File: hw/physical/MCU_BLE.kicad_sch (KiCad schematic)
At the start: 30 parts, among them SW201 RotaryEncoder_Switch, U1 nRF52840-QIAA, U5 MX25R3235FM1IL0, Y1 32M, Y2 32.768k

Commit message: - Consolidate POWER and BATTERY pages - Updated 1.8V SYS REG to low Iq option - Replaced LoRA module with SemTech transceiver - Adding latest nRF datasheet
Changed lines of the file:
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@@
 		(dnp no)
 		(property "Reference" "U1"
-			(at 199.39 57.15 0)
+			(at 202.946 60.452 0)
 			(effects
 				(font
@@
 		)
 		(property "Value" "nRF52840-QIAA"
-			(at 199.39 59.69 0)
+			(at 202.946 62.992 0)
 			(effects
 				(font

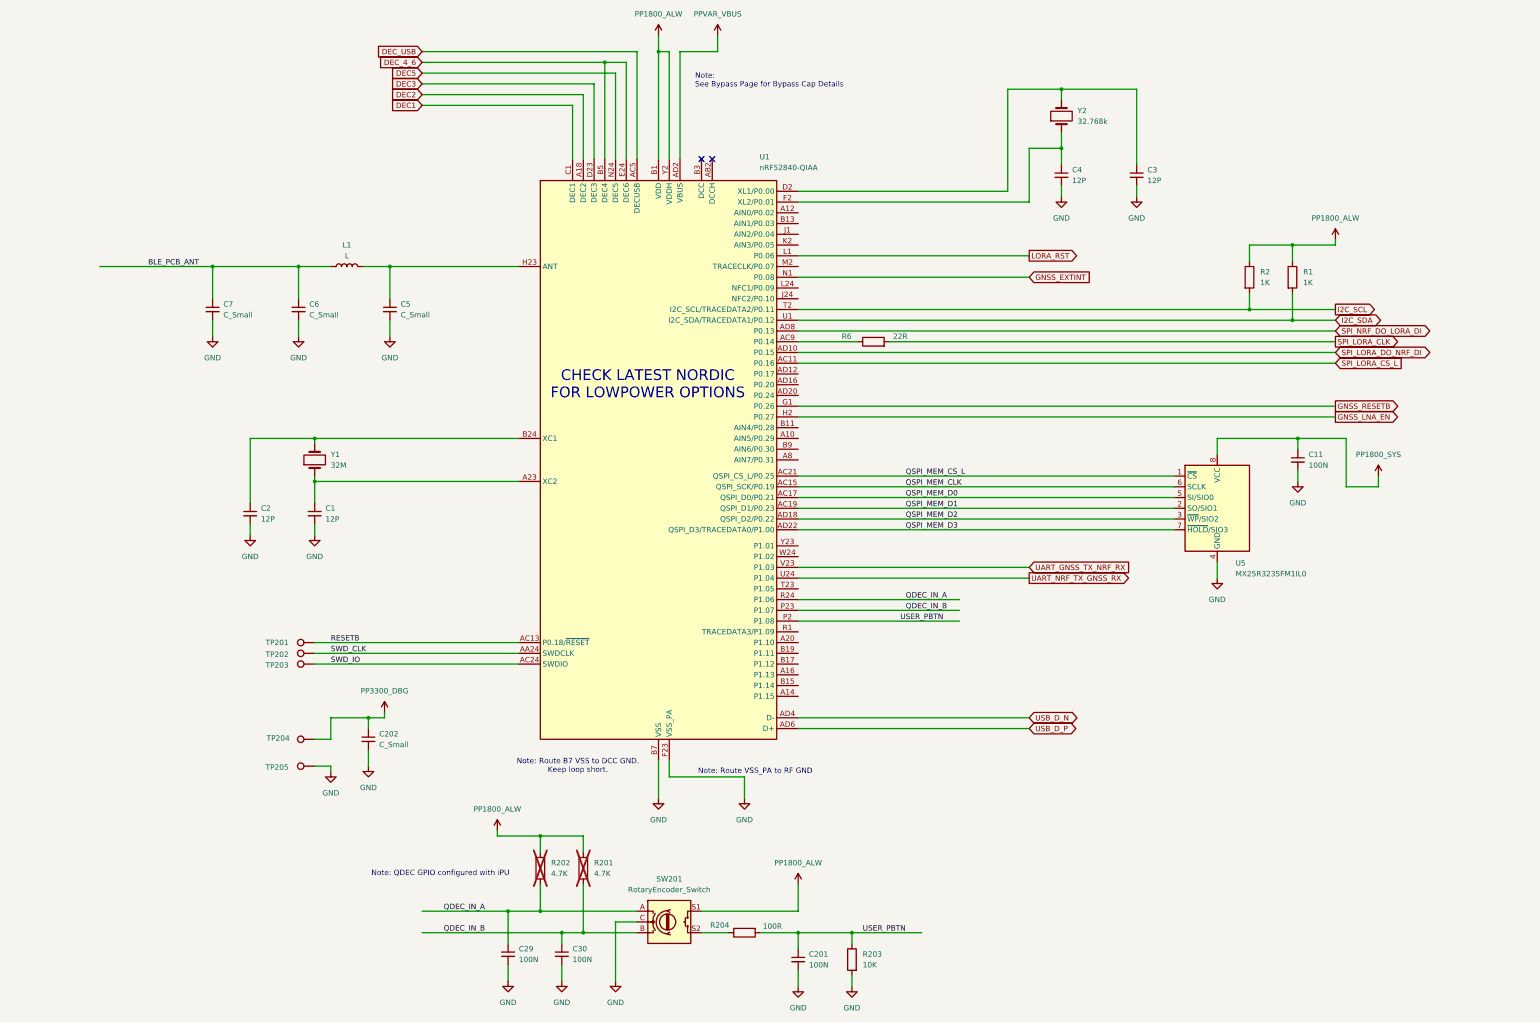
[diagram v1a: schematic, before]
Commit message: Adding nRF54L10 schematic library component. Redrew MCU page with nRF54L10 and rearranged or changed net labels and global labels.
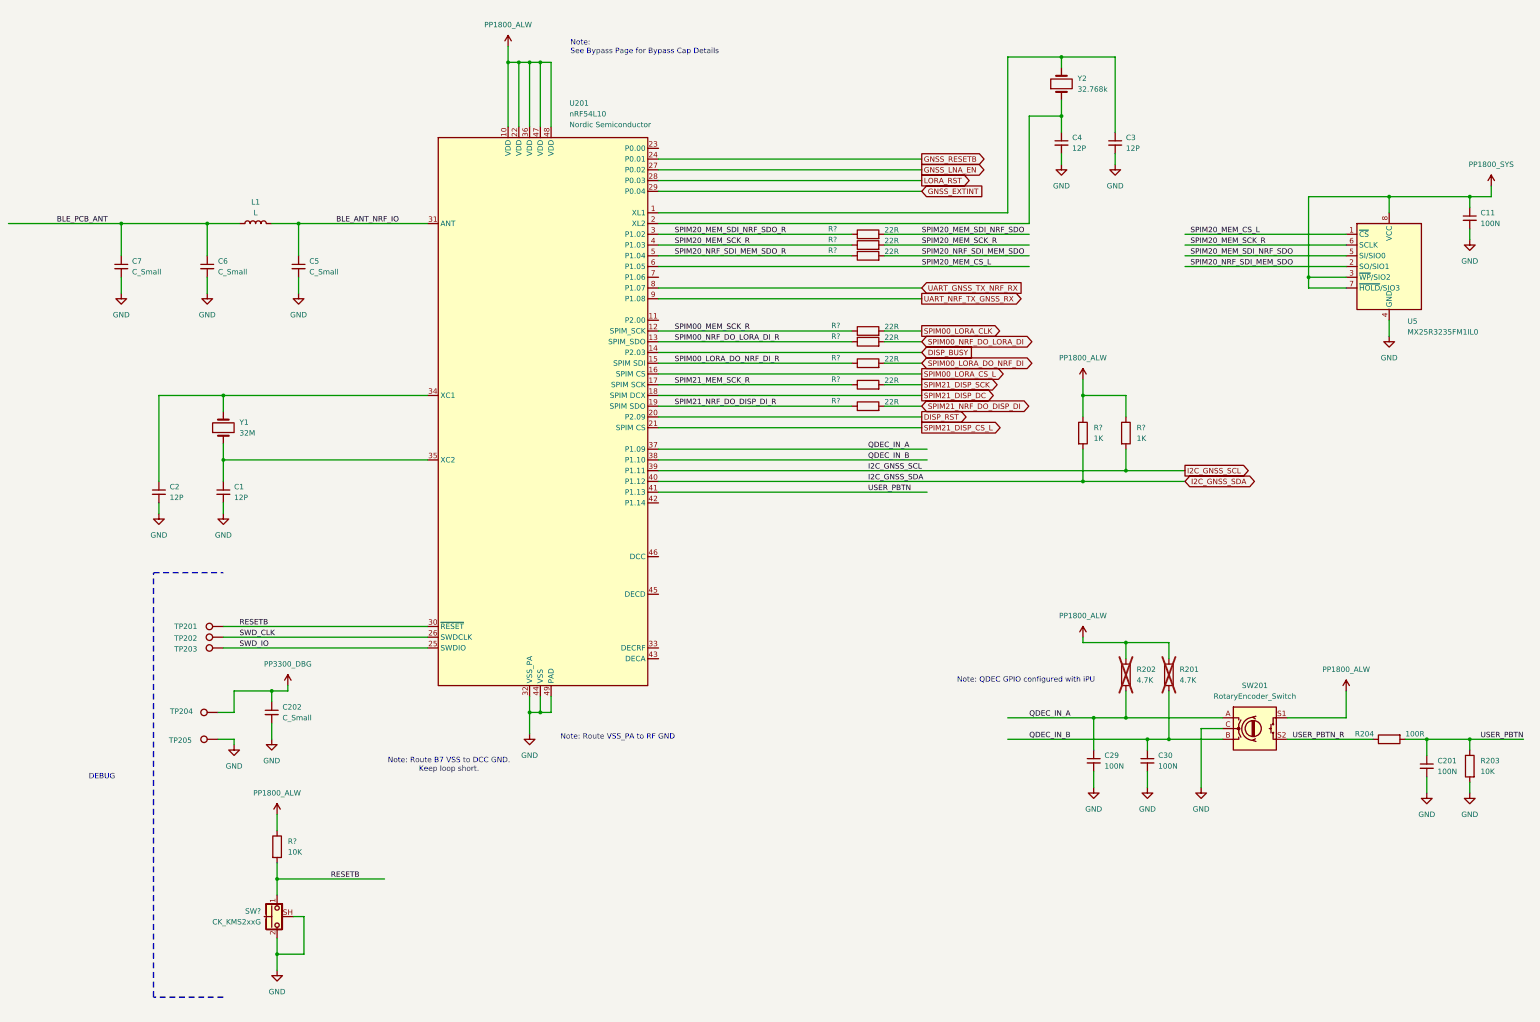
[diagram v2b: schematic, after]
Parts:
- removed R1, R2: 1K, symbol Device:R
- removed R6: 22R, symbol Device:R
- removed U1: nRF52840-QIAA, Package_DFN_QFN:Nordic_AQFN-73-1EP_7x7mm_P0.5mm, symbol MCU_Nordic:nRF52840
- added R? (x2): 1K, symbol Device:R
- added R? (x8): 22R, symbol Device:R
- added R?: 10K, symbol Device:R
- added SW?: CK_KMS2xxG, Button_Switch_SMD:SW_SPST_CK_KMS2xxGP, symbol Switch:CK_KMS2xxG
- added U201: nRF54L10, Package_DFN_QFN:QFN-48-1EP_6x6mm_P0.4mm_EP4.6x4.6mm, symbol nRF54L:nRF54L10
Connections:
- net QSPI_MEM_D2 is gone; now on net PP1800_SYS: U5.3 (~{WP}/SIO2)
- net QSPI_MEM_D3 is gone; now on net PP1800_SYS: U5.7 (~{HOLD}/SIO3)
- net GND: now also SW?.2, SW?.SH (B), U201.32 (VSS_PA), U201.44 (VSS), U201.49 (PAD)
- net GNSS_EXTINT: now also U201.29 (P0.04)
- net GNSS_LNA_EN: now also U201.27 (P0.02)
- net GNSS_RESETB: now also U201.24 (P0.01)
- net LORA_RST: now also U201.28 (P0.03)
- net PP1800_ALW: now also R?.1, R?.1, R?.1, U201.10 (VDD), U201.22 (VDD), U201.36 (VDD), U201.47 (VDD), U201.48 (VDD)
- net QDEC_IN_A: now also U201.37 (P1.09)
- net QDEC_IN_B: now also U201.38 (P1.10)
- net RESETB: now also R?.2, SW?.1, U201.30 (~{RESET})
- net SWD_CLK: now also U201.26 (SWDCLK)
- net SWD_IO: now also U201.25 (SWDIO)
- net UART_GNSS_TX_NRF_RX: now also U201.8 (P1.07)
- net UART_NRF_TX_GNSS_RX: now also U201.9 (P1.08)
- net USER_PBTN: now also U201.41 (P1.13)
- net at C1.1, Y1.1: now also U201.35 (XC2)
- net at C2.1, Y1.2: now also U201.34 (XC1)
- net at C3.1, Y2.2: now also U201.1 (P1.00)
- net at C4.1, Y2.1: now also U201.2 (P1.01)
- net BLE_ANT_NRF_IO: now reaches C5.1, L1.2
- net BLE_ANT_NRF_IO: now also U201.31 (ANT)
- net USER_PBTN_R: now reaches R204.1, SW201.S2
- net QSPI_MEM_CLK renamed SPIM20_MEM_SCK_R
- net SPIM20_MEM_SCK_R: now also R?.1, R?.2, U201.4 (P1.03)
- net QSPI_MEM_CS_L renamed SPIM20_MEM_CS_L
- net SPIM20_MEM_CS_L: now also U201.6 (P1.05)
- net QSPI_MEM_D0 renamed SPIM20_MEM_SDI_NRF_SDO
- net SPIM20_MEM_SDI_NRF_SDO: now also R?.2
- net QSPI_MEM_D1 renamed SPIM20_NRF_SDI_MEM_SDO
- net SPIM20_NRF_SDI_MEM_SDO: now also R?.2
- new net DISP_BUSY: U201.14 (P2.03)
- new net DISP_RST: U201.20 (P2.09)
- new net I2C_GNSS_SCL: R?.2, U201.39 (P1.11)
- new net I2C_GNSS_SDA: R?.2, U201.40 (P1.12)
- new net SPIM00_LORA_CLK: R?.2
- new net SPIM00_LORA_CS_L: U201.16 (P2.05)
- new net SPIM00_LORA_DO_NRF_DI: R?.2
- new net SPIM00_LORA_DO_NRF_DI_R: R?.1, U201.15 (P2.04)
- new net SPIM00_MEM_SCK_R: R?.1, U201.12 (P2.01)
- new net SPIM00_NRF_DO_LORA_DI: R?.2
- new net SPIM00_NRF_DO_LORA_DI_R: R?.1, U201.13 (P2.02)
- new net SPIM20_MEM_SDI_NRF_SDO_R: R?.1, U201.3 (P1.02)
- new net SPIM20_NRF_SDI_MEM_SDO_R: R?.1, U201.5 (P1.04)
- new net SPIM21_DISP_CS_L: U201.21 (P2.10)
- new net SPIM21_DISP_DC: U201.18 (P2.07)
- new net SPIM21_DISP_SCK: R?.2
- new net SPIM21_MEM_SCK_R: R?.1, U201.17 (P2.06)
- new net SPIM21_NRF_DO_DISP_DI: R?.2
- new net SPIM21_NRF_DO_DISP_DI_R: R?.1, U201.19 (P2.08)
- no-connect marks 2 -> 0
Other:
- note added: "DEBUG"
- note removed: "CHECK LATEST NORDIC FOR LOWPOWER OPTIONS"
- moved on the sheet: C1, C11, C2, C201, C202, C29, C3, C30, C4, C5, C6, C7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

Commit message: Various Schematic Modifications and Additions. * Removed Bypass page and moved bypass caps to MCU page. * Moved MCU VSS_PA pin to logical location as per Nordic guidelines. * Added Display Circuit, level shifters, charge pump, connector, etc. * Added 3.3V display VREG with Enable GPIO. * Added BLE RF components as per Nordic guidelines. * Added DCC circuit as per Nordic guidelines. * Rearranged GPIO's and interfaces. * Fixed various schematic errors.
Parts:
- removed C7: C_Small, symbol Device:C_Small
- removed L1: L, symbol Device:L
- added C201: 4.7UF, symbol Device:C_Small
- added C202: 1UF, symbol Device:C_Small
- added C203, C204, C205, C206, C207: 100NF, symbol Device:C_Small
- added C213: 1.5P, Capacitor_SMD:C_0201_0603Metric, symbol Device:C_Small
- added C216, C219: 2.2U, symbol Device:C_Small
- added C217, C218: 10N, symbol Device:C_Small
- added C224: 3.9P, symbol Device:C_Small
- added L201, L202: 3.5N, Inductor_SMD:L_0201_0603Metric, symbol Device:L
- added L203: 2.7N, Inductor_SMD:L_0201_0603Metric, symbol Device:L
- added L204: 4.7U, symbol Device:L
- added L205: L, symbol Device:L
- C211: renamed from C6; value C_Small -> 0.3P
- C212: renamed from C5; value C_Small -> 2.0P; footprint (none) -> Capacitor_SMD:C_0201_0603Metric; MFG_PN (none) -> GJM0335C1E2R0WB01
- C223: renamed from C202; value C_Small -> 4.7U
- R213: renamed from R?; value 10K -> 1K
- gave numbers to parts that had none: 11
- renumbered C4 to C208, C3 to C209, C11 to C210, C2 to C214, C1 to C215, C29 to C220, C30 to C221, C201 to C222, R202 to R211, R201 to R212, R204 to R214, R203 to R215, U5 to U202, Y2 to Y201, Y1 to Y202
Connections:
- net BLE_PCB_ANT: now also L201.1
- net GND: now also C201.2, C202.2, C203.2, C204.2, C205.2, C206.2, C207.2, C213.2, C216.2, C217.2, C218.2, C219.2, C224.2
- net LORA_RST: now also U201.23 (P0.00); no longer U201.28 (P0.03)
- net PP1800_ALW: now also C201.1, C202.1, C203.1, C204.1, C205.1, C206.1, C207.1
- net RESETB: now also C224.1
- net DISP_VREG_EN: now reaches U201.11 (P2.00)
- net at U201.33 (DECRF): now also U201.43 (DECA), C217.1, C218.1, C219.1, L205.2
- net XC1: now reaches C214.1, U201.34 (XC1), Y202.2
- net XC2: now reaches C215.1, U201.35 (XC2), Y202.1
- net BAT_CHRG_PG_L: now reaches U201.42 (P1.14)
- net at U201.45 (DECD): now also C216.1, L204.2, L205.1
- net at U201.46 (DCC): now also L204.1
- net BAT_CHRG_TTDM: now reaches U201.7 (P1.06)
- net BLE_ANT_NRF_IO renamed RF2
- net RF2: now also L201.2, L202.1; no longer U201.31 (ANT)
- new net DISP_EN: U201.28 (P0.03)
- new net RF1: C213.1, L202.2, L203.1
- new net RF_BLE_ANT_NRF_IO: L203.2, U201.31 (ANT)
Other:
- note added: "BLE MCU"
- note added: "Note: RF GND"
- note added: "Note: VSS_PA to GND PAD ONLY!"
- note removed: "Note: Route B7 VSS to DCC GND. Keep loop short."
- note removed: "Note: Route VSS_PA to RF GND"
- moved on the sheet: C208, C209, C210, C211, C212, C214, C215, C220, C221, C222, C223, R201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
